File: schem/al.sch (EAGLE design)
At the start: 17 parts, among them IC1 74163N, IC10 74HC377N, IC11 74HC244N, IC12 74HC244N, IC13 74HC244N, IC14 74HC377N, IC15 74HC244N, IC16 74HC244N, IC17 74HC244N, IC2 74163N, IC3 74163N, IC4 74163N, IC5 74HC138N, IC6 74HC244N, IC7 74HC244N, IC8 74HC244N, IC9 74HC244N

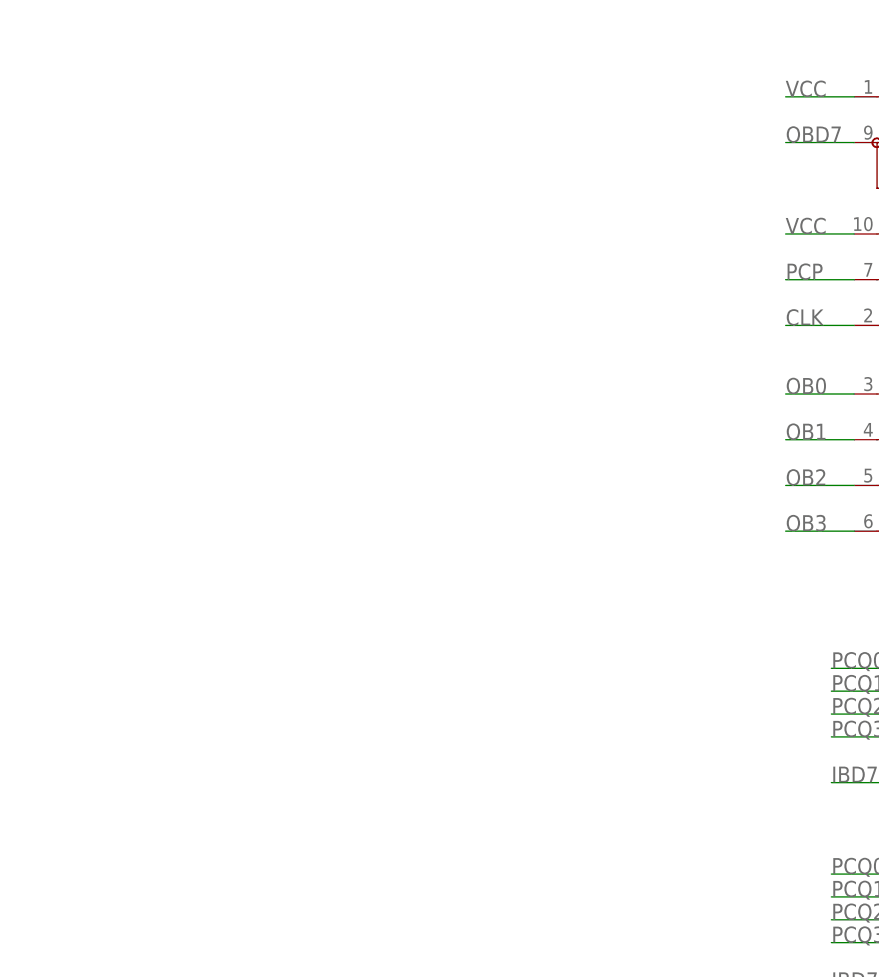
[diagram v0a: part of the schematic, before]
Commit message: finished most schematics
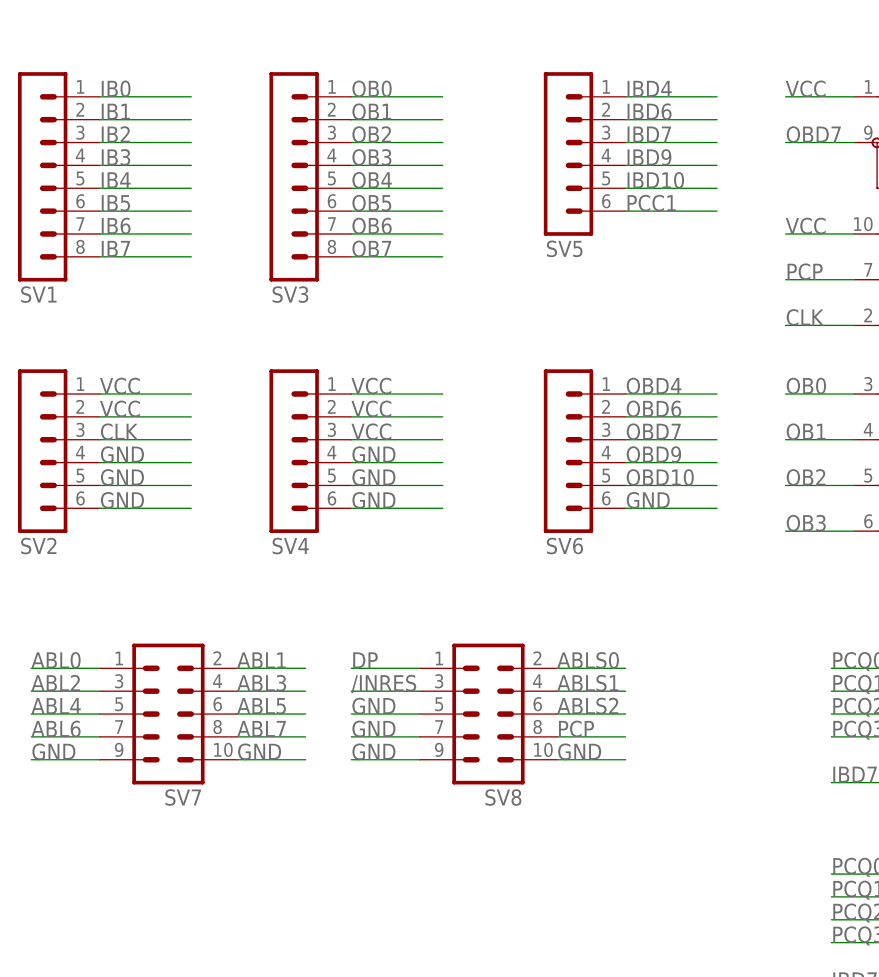
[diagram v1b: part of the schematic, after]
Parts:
- added SV1, SV3: (no value), con-lstb:MA08-1
- added SV2, SV4, SV5, SV6: (no value), con-lstb:MA06-1
- added SV7, SV8: (no value), con-lstb:MA05-2
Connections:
- new net IBD10: SV5.5
- new net OBD10: SV6.5
- net /INRES: now also SV8.3
- net ABL0: now also SV7.1
- net ABL1: now also SV7.2
- net ABL2: now also SV7.3
- net ABL3: now also SV7.4
- net ABL4: now also SV7.5
- net ABL5: now also SV7.6
- net ABL6: now also SV7.7
- net ABL7: now also SV7.8
- net ABLS0: now also SV8.2
- net ABLS1: now also SV8.4
- net ABLS2: now also SV8.6
- net CLK: now also SV2.3
- net DP: now also SV8.1
- net GND: now also SV2.4, SV2.5, SV2.6, SV4.4, SV4.5, SV4.6, SV6.6, SV7.10, SV7.9, SV8.10, SV8.5, SV8.7, SV8.9
- net IB0: now also SV1.1
- net IB1: now also SV1.2
- net IB2: now also SV1.3
- net IB3: now also SV1.4
- net IB4: now also SV1.5
- net IB5: now also SV1.6
- net IB6: now also SV1.7
- net IB7: now also SV1.8
- net IBD4: now also SV5.1
- net IBD6: now also SV5.2
- net IBD7: now also SV5.3
- net IBD9: now also SV5.4
- net OB0: now also SV3.1
- net OB1: now also SV3.2
- net OB2: now also SV3.3
- net OB3: now also SV3.4
- net OB4: now also SV3.5
- net OB5: now also SV3.6
- net OB6: now also SV3.7
- net OB7: now also SV3.8
- net OBD4: now also SV6.1
- net OBD6: now also SV6.2
- net OBD7: now also SV6.3
- net OBD9: now also SV6.4
- net PCC1: now also SV5.6
- net PCP: now also SV8.8
- net VCC: now also SV2.1, SV2.2, SV4.1, SV4.2, SV4.3

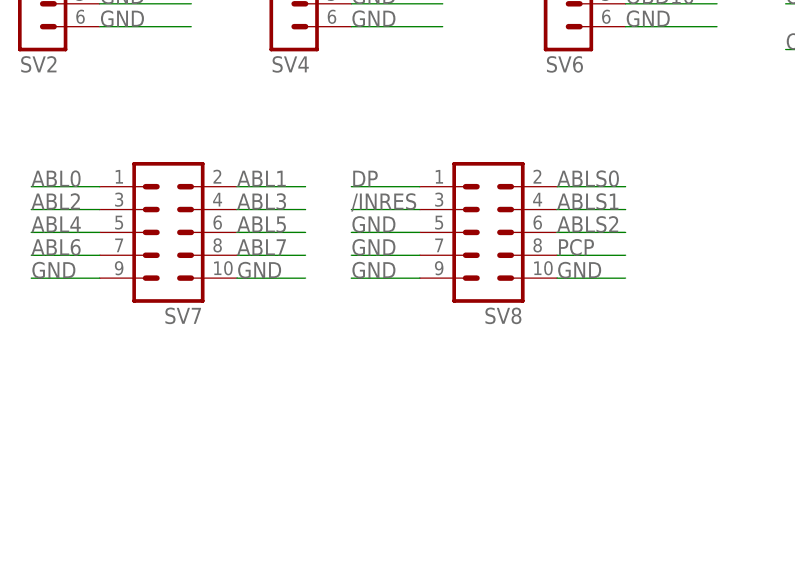
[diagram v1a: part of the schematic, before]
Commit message: adapted schematics for single headers
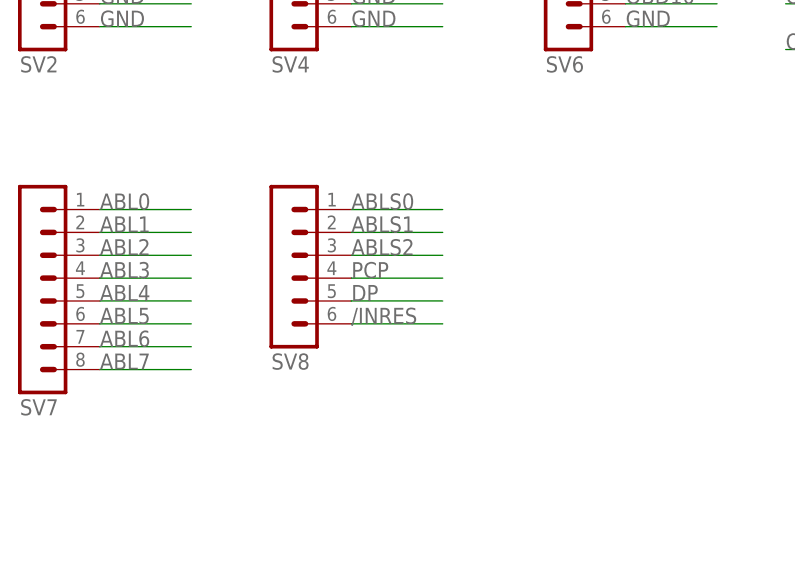
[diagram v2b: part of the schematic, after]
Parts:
- SV7: device con-lstb:MA05-2 -> con-lstb:MA08-1
- SV8: device con-lstb:MA05-2 -> con-lstb:MA06-1
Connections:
- net /INRES: now also SV8.6; no longer SV8.3
- net ABLS0: now also SV8.1; no longer SV8.2
- net ABLS1: now also SV8.2; no longer SV8.4
- net ABLS2: now also SV8.3; no longer SV8.6
- net DP: now also SV8.5; no longer SV8.1
- net GND: no longer SV7.10, SV7.9, SV8.10, SV8.5, SV8.7, SV8.9
- net PCP: now also SV8.4; no longer SV8.8
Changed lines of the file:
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@@
 <part name="SV5" library="con-lstb" deviceset="MA06-1" device=""/>
 <part name="SV6" library="con-lstb" deviceset="MA06-1" device=""/>
-<part name="SV7" library="con-lstb" deviceset="MA05-2" device=""/>
-<part name="SV8" library="con-lstb" deviceset="MA05-2" device=""/>
+<part name="SV7" library="con-lstb" deviceset="MA08-1" device=""/>
+<part name="SV8" library="con-lstb" deviceset="MA06-1" device=""/>
 </parts>
 <sheets>
@@
 <instance part="SV5" gate="1" x="-25.4" y="83.82" rot="MR180"/>
 <instance part="SV6" gate="1" x="-25.4" y="50.8" rot="MR180"/>
-<instance part="SV7" gate="G$1" x="-68.58" y="22.86" rot="R180"/>
-<instance part="SV8" gate="G$1" x="-33.02" y="22.86" rot="R180"/>
+<instance part="SV7" gate="1" x="-83.82" y="17.78" rot="MR180"/>
+<instance part="SV8" gate="1" x="-55.88" y="17.78" rot="MR180"/>
 </instances>
 <busses>
@@
 </segment>
 <segment>
-<pinref part="SV8" gate="G$1" pin="8"/>
-<wire x1="-25.4" y1="20.32" x2="-17.78" y2="20.32" width="0.1524" layer="91"/>
-<label x="-25.4" y="20.32" size="1.778" layer="95"/>
+<pinref part="SV8" gate="1" pin="4"/>
+<wire x1="-48.26" y1="17.78" x2="-38.1" y2="17.78" width="0.1524" layer="91"/>
+<label x="-48.26" y="17.78" size="1.778" layer="95"/>
 </segment>
 </net>
@@
 </segment>
 <segment>
-<pinref part="SV8" gate="G$1" pin="1"/>
-<wire x1="-40.64" y1="27.94" x2="-48.26" y2="27.94" width="0.1524" layer="91"/>
-<label x="-48.26" y="27.94" size="1.778" layer="95"/>
+<pinref part="SV8" gate="1" pin="5"/>
+<wire x1="-48.26" y1="15.24" x2="-38.1" y2="15.24" width="0.1524" layer="91"/>
+<label x="-48.26" y="15.24" size="1.778" layer="95"/>
 </segment>
 </net>
@@
 </segment>
 <segment>
-<pinref part="SV8" gate="G$1" pin="2"/>
-<wire x1="-25.4" y1="27.94" x2="-17.78" y2="27.94" width="0.1524" layer="91"/>
-<label x="-25.4" y="27.94" size="1.778" layer="95"/>
+<pinref part="SV8" gate="1" pin="1"/>
+<wire x1="-48.26" y1="25.4" x2="-38.1" y2="25.4" width="0.1524" layer="91"/>
+<label x="-48.26" y="25.4" size="1.778" layer="95"/>
 </segment>
 </net>
@@
 </segment>
 <segment>
-<pinref part="SV8" gate="G$1" pin="4"/>
-<wire x1="-25.4" y1="25.4" x2="-17.78" y2="25.4" width="0.1524" layer="91"/>
-<label x="-25.4" y="25.4" size="1.778" layer="95"/>
+<pinref part="SV8" gate="1" pin="2"/>
+<wire x1="-48.26" y1="22.86" x2="-38.1" y2="22.86" width="0.1524" layer="91"/>
+<label x="-48.26" y="22.86" size="1.778" layer="95"/>
 </segment>
 </net>
@@
 </segment>
 <segment>
-<pinref part="SV8" gate="G$1" pin="6"/>
-<wire x1="-25.4" y1="22.86" x2="-17.78" y2="22.86" width="0.1524" layer="91"/>
-<label x="-25.4" y="22.86" size="1.778" layer="95"/>
+<pinref part="SV8" gate="1" pin="3"/>
+<wire x1="-48.26" y1="20.32" x2="-38.1" y2="20.32" width="0.1524" layer="91"/>
+<label x="-48.26" y="20.32" size="1.778" layer="95"/>
 </segment>
 </net>
@@
 <label x="-17.78" y="45.72" size="1.778" layer="95"/>
 </segment>
-<segment>
-<pinref part="SV7" gate="G$1" pin="9"/>
-<wire x1="-76.2" y1="17.78" x2="-83.82" y2="17.78" width="0.1524" layer="91"/>
-<label x="-83.82" y="17.78" size="1.778" layer="95"/>
-</segment>
-<segment>
-<pinref part="SV7" gate="G$1" pin="10"/>
-<wire x1="-60.96" y1="17.78" x2="-53.34" y2="17.78" width="0.1524" layer="91"/>
-<label x="-60.96" y="17.78" size="1.778" layer="95"/>
-</segment>
-<segment>
-<pinref part="SV8" gate="G$1" pin="5"/>
-<wire x1="-48.26" y1="22.86" x2="-40.64" y2="22.86" width="0.1524" layer="91"/>
-<label x="-48.26" y="22.86" size="1.778" layer="95"/>
-</segment>
-<segment>
-<pinref part="SV8" gate="G$1" pin="7"/>
-<wire x1="-40.64" y1="20.32" x2="-48.26" y2="20.32" width="0.1524" layer="91"/>
-<label x="-48.26" y="20.32" size="1.778" layer="95"/>
-</segment>
-<segment>
-<pinref part="SV8" gate="G$1" pin="9"/>
-<wire x1="-48.26" y1="17.78" x2="-40.64" y2="17.78" width="0.1524" layer="91"/>
-<label x="-48.26" y="17.78" size="1.778" layer="95"/>
-</segment>
-<segment>
-<pinref part="SV8" gate="G$1" pin="10"/>
-<wire x1="-25.4" y1="17.78" x2="-17.78" y2="17.78" width="0.1524" layer="91"/>
-<label x="-25.4" y="17.78" size="1.778" layer="95"/>
-</segment>
 </net>
 <net name="ABLD0" class="0">
@@
 </segment>
 <segment>
-<pinref part="SV7" gate="G$1" pin="1"/>
-<wire x1="-76.2" y1="27.94" x2="-83.82" y2="27.94" width="0.1524" layer="91"/>
-<label x="-83.82" y="27.94" size="1.778" layer="95"/>
+<pinref part="SV7" gate="1" pin="1"/>
+<wire x1="-76.2" y1="25.4" x2="-66.04" y2="25.4" width="0.1524" layer="91"/>
+<label x="-76.2" y="25.4" size="1.778" layer="95"/>
 </segment>
 </net>
@@
 </segment>
 <segment>
-<pinref part="SV7" gate="G$1" pin="2"/>
-<wire x1="-60.96" y1="27.94" x2="-53.34" y2="27.94" width="0.1524" layer="91"/>
-<label x="-60.96" y="27.94" size="1.778" layer="95"/>
+<pinref part="SV7" gate="1" pin="2"/>
+<wire x1="-76.2" y1="22.86" x2="-66.04" y2="22.86" width="0.1524" layer="91"/>
+<label x="-76.2" y="22.86" size="1.778" layer="95"/>
 </segment>
 </net>
@@
 </segment>
 <segment>
-<pinref part="SV7" gate="G$1" pin="3"/>
-<wire x1="-83.82" y1="25.4" x2="-76.2" y2="25.4" width="0.1524" layer="91"/>
-<label x="-83.82" y="25.4" size="1.778" layer="95"/>
+<pinref part="SV7" gate="1" pin="3"/>
+<wire x1="-76.2" y1="20.32" x2="-66.04" y2="20.32" width="0.1524" layer="91"/>
+<label x="-76.2" y="20.32" size="1.778" layer="95"/>
 </segment>
 </net>
@@
 </segment>
 <segment>
-<pinref part="SV7" gate="G$1" pin="4"/>
-<wire x1="-60.96" y1="25.4" x2="-53.34" y2="25.4" width="0.1524" layer="91"/>
-<label x="-60.96" y="25.4" size="1.778" layer="95"/>
+<pinref part="SV7" gate="1" pin="4"/>
+<wire x1="-76.2" y1="17.78" x2="-66.04" y2="17.78" width="0.1524" layer="91"/>
+<label x="-76.2" y="17.78" size="1.778" layer="95"/>
 </segment>
 </net>
@@
 </segment>
 <segment>
-<pinref part="SV7" gate="G$1" pin="5"/>
-<wire x1="-76.2" y1="22.86" x2="-83.82" y2="22.86" width="0.1524" layer="91"/>
-<label x="-83.82" y="22.86" size="1.778" layer="95"/>
+<pinref part="SV7" gate="1" pin="5"/>
+<wire x1="-76.2" y1="15.24" x2="-66.04" y2="15.24" width="0.1524" layer="91"/>
+<label x="-76.2" y="15.24" size="1.778" layer="95"/>
 </segment>
 </net>
@@
 </segment>
 <segment>
-<pinref part="SV7" gate="G$1" pin="6"/>
-<wire x1="-60.96" y1="22.86" x2="-53.34" y2="22.86" width="0.1524" layer="91"/>
-<label x="-60.96" y="22.86" size="1.778" layer="95"/>
+<pinref part="SV7" gate="1" pin="6"/>
+<wire x1="-76.2" y1="12.7" x2="-66.04" y2="12.7" width="0.1524" layer="91"/>
+<label x="-76.2" y="12.7" size="1.778" layer="95"/>
 </segment>
 </net>
@@
 </segment>
 <segment>
-<pinref part="SV7" gate="G$1" pin="7"/>
-<wire x1="-83.82" y1="20.32" x2="-76.2" y2="20.32" width="0.1524" layer="91"/>
-<label x="-83.82" y="20.32" size="1.778" layer="95"/>
+<pinref part="SV7" gate="1" pin="7"/>
+<wire x1="-76.2" y1="10.16" x2="-66.04" y2="10.16" width="0.1524" layer="91"/>
+<label x="-76.2" y="10.16" size="1.778" layer="95"/>
 </segment>
 </net>
@@
 </segment>
 <segment>
-<pinref part="SV7" gate="G$1" pin="8"/>
-<wire x1="-60.96" y1="20.32" x2="-53.34" y2="20.32" width="0.1524" layer="91"/>
-<label x="-60.96" y="20.32" size="1.778" layer="95"/>
+<pinref part="SV7" gate="1" pin="8"/>
+<wire x1="-76.2" y1="7.62" x2="-66.04" y2="7.62" width="0.1524" layer="91"/>
+<label x="-76.2" y="7.62" size="1.778" layer="95"/>
 </segment>
 </net>
@@
 </segment>
 <segment>
-<pinref part="SV8" gate="G$1" pin="3"/>
-<wire x1="-40.64" y1="25.4" x2="-48.26" y2="25.4" width="0.1524" layer="91"/>
-<label x="-48.26" y="25.4" size="1.778" layer="95"/>
-</segment>
-</net>
+<pinref part="SV8" gate="1" pin="6"/>
+<wire x1="-48.26" y1="12.7" x2="-38.1" y2="12.7" width="0.1524" layer="91"/>
+<label x="-48.26" y="12.7" size="1.778" layer="95"/>
+</segment>
+</net>

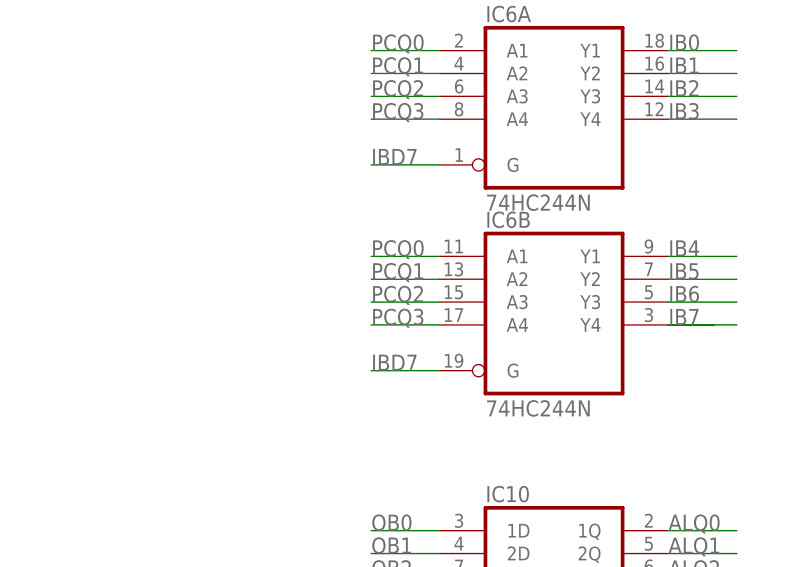
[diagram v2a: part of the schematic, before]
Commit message: mistakes in boards fixed
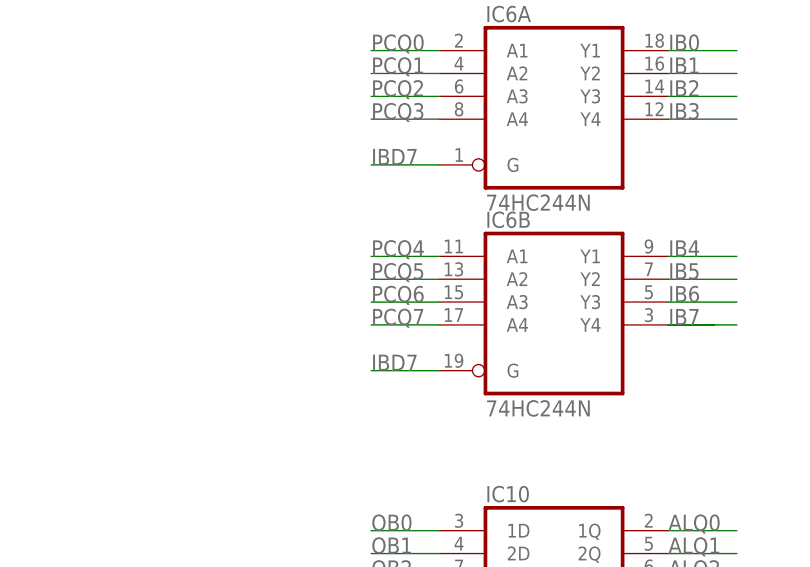
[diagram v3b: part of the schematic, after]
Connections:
- net PCQ0: no longer IC6B.A1
- net PCQ1: no longer IC6B.A2
- net PCQ2: no longer IC6B.A3
- net PCQ3: no longer IC6B.A4
- net PCQ4: now also IC6B.A1
- net PCQ5: now also IC6B.A2
- net PCQ6: now also IC6B.A3
- net PCQ7: now also IC6B.A4
